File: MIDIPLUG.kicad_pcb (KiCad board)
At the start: 4 copper layers, 24.4 x 31.1 mm, 31 parts, among them J1 Joystick Port, P1 LINE OUT, U1 LP2985-3.3, U2 SAM2695, Y1 12Mhz

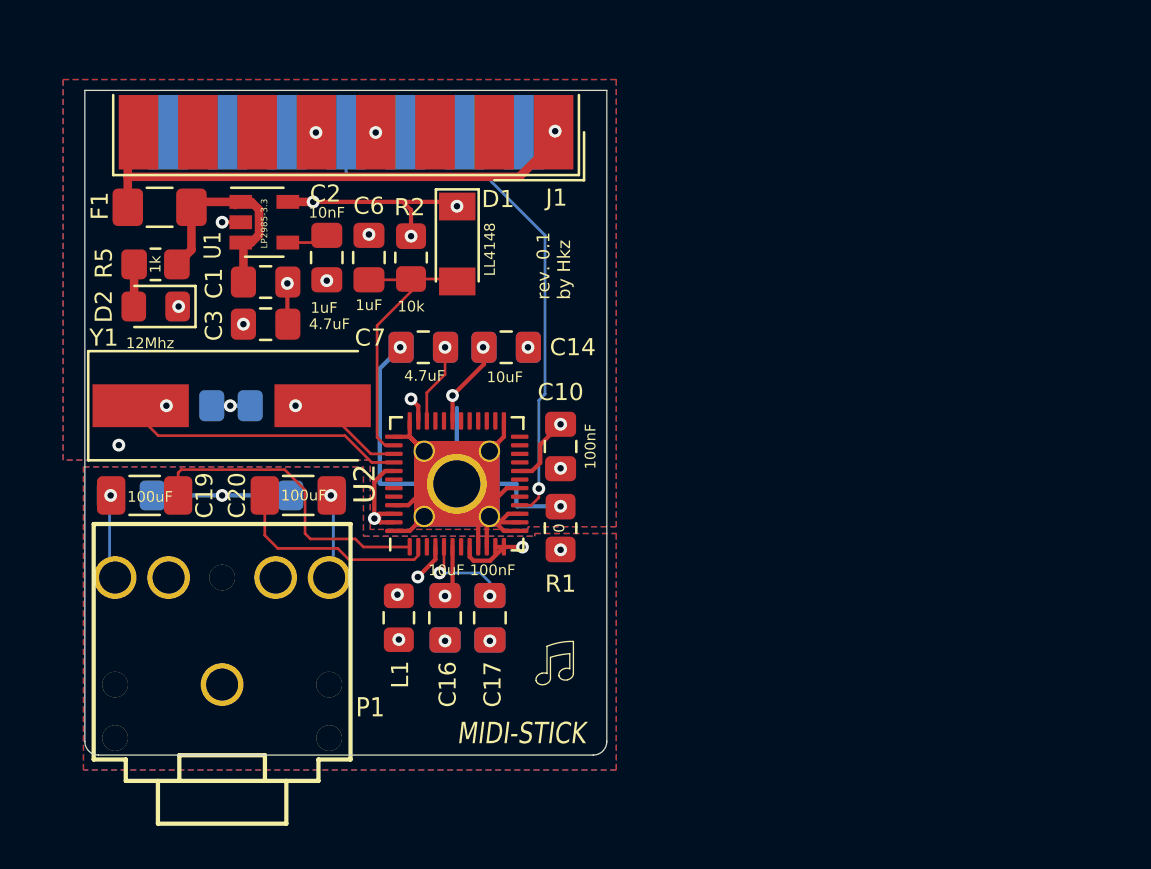
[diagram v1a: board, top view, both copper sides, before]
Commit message: Begin reorganizing board
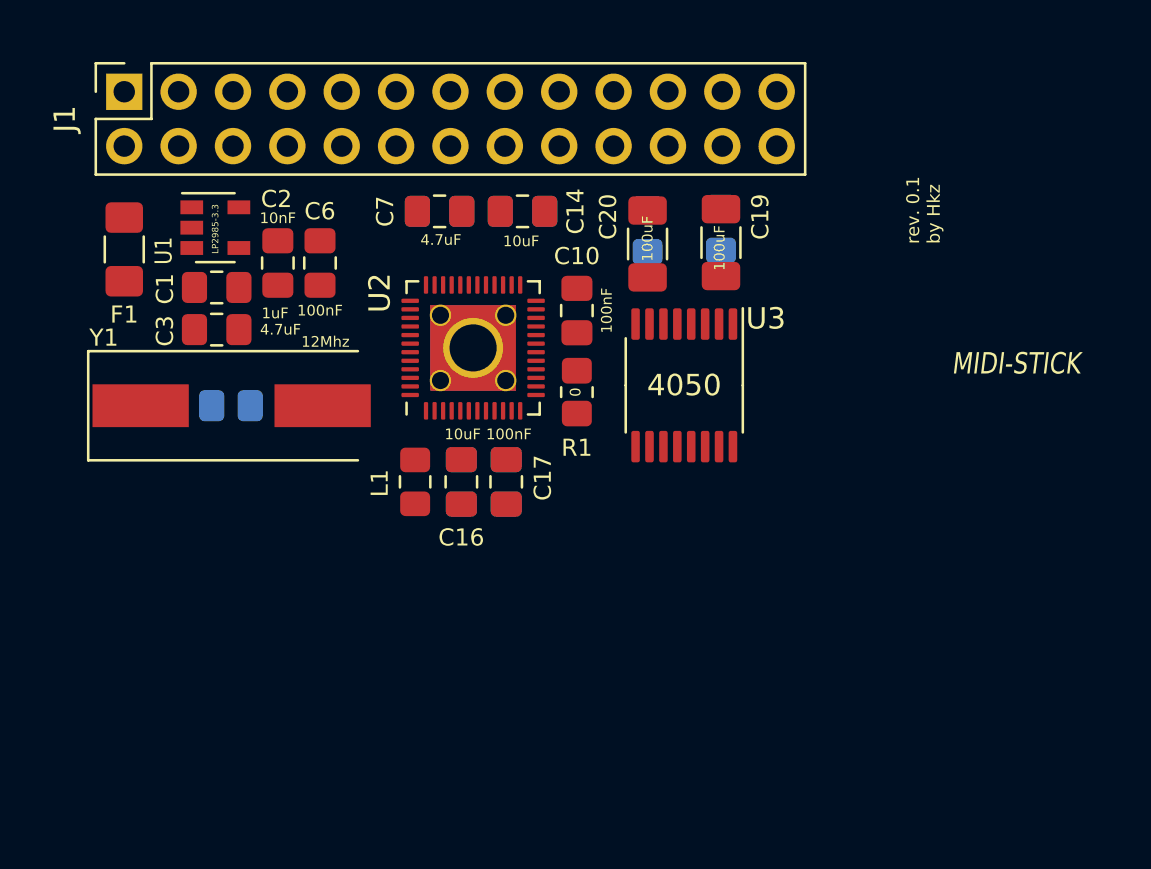
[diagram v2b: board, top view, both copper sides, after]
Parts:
- removed D1: LL4148, Diode_SMD:D_MiniMELF
- removed D2: Power, LED_SMD:LED_0805_2012Metric_Pad1.15x1.40mm_HandSolder
- removed P1: LINE OUT, My_Components:Conn_Audio_3.5mm_Stereo_SJ1-352XNG
- removed R2: 10k, Resistor_SMD:R_0805_2012Metric_Pad1.20x1.40mm_HandSolder
- removed R5: 1k, Resistor_SMD:R_0805_2012Metric_Pad1.20x1.40mm_HandSolder
- added U3: 4050, Package_SO:TSSOP-16_4.4x5mm_P0.65mm, F.Cu at (134.6, 88.1)
- C6: value 1uF -> 100nF
- J1: value Joystick Port -> Wavetable Connector; footprint Connector_Dsub:DSUB-15_Male_EdgeMount_P2.77mm -> Connector_PinSocket_2.54mm:PinSocket_2x13_P2.54mm_Vertical
- moved R4 30.2 mm to (136.3, 80.8), turned to 270 degrees
- moved C19 29.4 mm to (136.3, 81.5), turned to 90 degrees
- moved C20 20.1 mm to (132.9, 81.5), turned to 90 degrees
- moved R3 20.0 mm to (132.9, 80.9), turned to 270 degrees
- moved J1 10.5 mm to (108.5, 74.4), turned to 90 degrees
- moved C10 6.40 mm to (129.6, 84.6)
- moved U2 6.40 mm to (124.8, 86.4)
- moved C14 6.40 mm to (127.1, 80.0)
- moved C15 6.40 mm to (124.2, 92.6)
- moved C16 6.40 mm to (124.2, 92.6)
- moved C17 6.40 mm to (126.3, 92.6)
- moved C18 6.40 mm to (126.3, 92.6)
- moved C7 6.40 mm to (123.2, 80.0)
- moved C8 6.40 mm to (123.2, 80.0)
- moved C9 6.40 mm to (127.1, 80.0)
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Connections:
- C19 pad 2: Net-(C19-Pad2) -> /AOUT_L
- C20 pad 2: Net-(C20-Pad2) -> /AOUT_R
- J1 pad 1: VCC -> GND
- J1 pad 10: (no net) -> VCC
- J1 pad 11: (no net) -> GND
- J1 pad 12: /MIDI_IN -> (no net)
- J1 pad 14: (no net) -> VCC
- J1 pad 3: (no net) -> GND
- J1 pad 4: GND -> /MIDI_IN
- J1 pad 6: (no net) -> VCC
- J1 pad 7: (no net) -> GND
- J1 pad 8: VCC -> (no net)
- J1 pad 9: VCC -> GND
- R3 pad 1: Net-(C20-Pad2) -> /AOUT_R
- R4 pad 1: Net-(C19-Pad2) -> /AOUT_L
- U2 pad 16: /MIDI_IN -> Net-(U2-Pad16)
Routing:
- net GND: track 114.5 -> 0.00 mm, vias 13 -> 0
- net VDD: track 76.2 -> 0.00 mm, vias 11 -> 0
- net GNDA: track 39.5 -> 0.00 mm, vias 5 -> 0
- net VCC: track 26.2 -> 0.00 mm, vias 1 -> 0
- net /MIDI_IN: track 25.8 -> 0.00 mm, vias 1 -> 0
- net Net-(C19-Pad1): track 15.2 -> 0.00 mm
- net Net-(C5-Pad1): track 13.3 -> 0.00 mm, vias 1 -> 0
- net Net-(C6-Pad1): track 13.2 -> 0.00 mm
- net Net-(C1-Pad1): track 11.6 -> 0.00 mm
- net Net-(C20-Pad1): track 10.8 -> 0.00 mm
- net VDDA: track 5.85 -> 0.00 mm, vias 2 -> 0
- net Net-(C17-Pad1): track 4.44 -> 0.00 mm, vias 2 -> 0
- net Net-(C4-Pad1): track 4.25 -> 0.00 mm, vias 1 -> 0
- net Net-(C19-Pad2): track 3.94 -> 0.00 mm, vias 1 -> 0
- net Net-(C20-Pad2): track 3.91 -> 0.00 mm, vias 1 -> 0
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- removed copper zone on B.Cu, net GND
- removed copper zone on F.Cu, net GND
- removed copper zone on In1.Cu, net GND
- removed copper zone on B.Cu, net GNDA
- removed copper zone on F.Cu, net GNDA
- removed copper zone on In1.Cu, net GNDA
- removed copper zone on In2.Cu, net GNDA
- removed copper zone on In2.Cu, net VDD
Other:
- board outline removed

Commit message: Routed internal version
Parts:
- moved R1 2.22 mm to (129.6, 90.7)
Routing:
- net GND: track 0.00 -> 107.3 mm, vias 0 -> 6
- net VDD: track 0.00 -> 80.8 mm, vias 0 -> 7
- net GNDA: track 0.00 -> 47.0 mm, vias 0 -> 2
- net Net-(C20-Pad1): track 0.00 -> 42.0 mm, vias 0 -> 2
- net Net-(C19-Pad1): track 0.00 -> 40.5 mm, vias 0 -> 2
- net /MIDI_IN: track 0.00 -> 29.9 mm
- net Net-(C6-Pad1): track 0.00 -> 22.9 mm, vias 0 -> 2
- net VCC: track 0.00 -> 21.7 mm
- net Net-(C5-Pad1): track 0.00 -> 17.5 mm, vias 0 -> 1
- net /~RESET_5V: track 0.00 -> 14.7 mm
- net VDDA: track 0.00 -> 10.6 mm, vias 0 -> 2
- net Net-(U2-Pad16): track 0.00 -> 9.31 mm, vias 0 -> 2
- net Net-(C1-Pad1): track 0.00 -> 9.22 mm
- net Net-(C17-Pad1): track 0.00 -> 7.68 mm, vias 0 -> 2
- net Net-(C4-Pad1): track 0.00 -> 6.83 mm, vias 0 -> 1
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- added copper zone on B.Cu, net GND
- added copper zone on F.Cu, net GND
- added copper zone on B.Cu, net GNDA
- added copper zone on F.Cu, net GNDA
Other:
- board outline added: 34 x 23.4 mm
- copper layers 4 -> 2
- board text added: "DWAVE"
- board text removed: "MIDI-STICK"

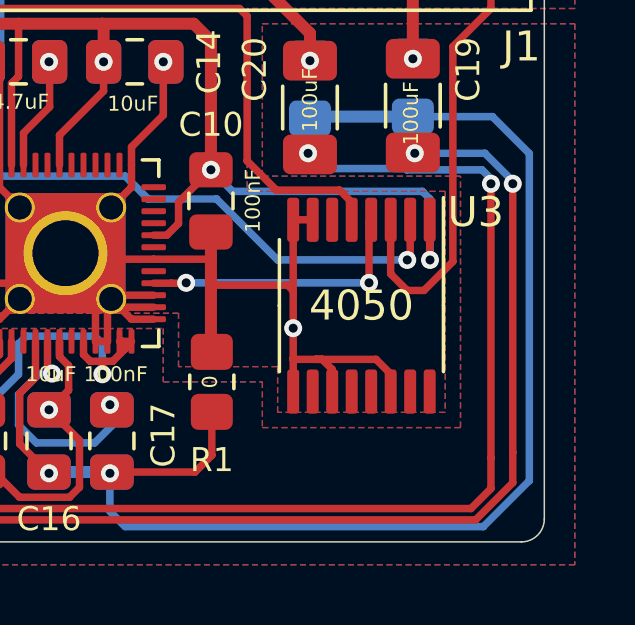
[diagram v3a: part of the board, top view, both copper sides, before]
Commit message: Add bypass cap for 4050
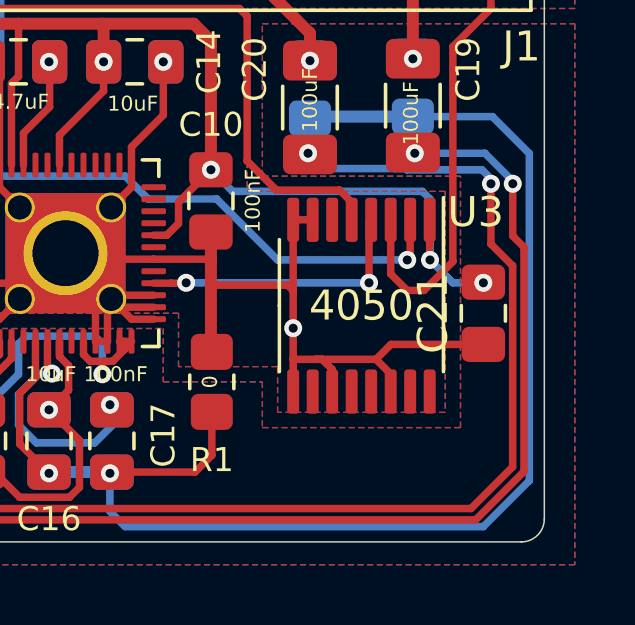
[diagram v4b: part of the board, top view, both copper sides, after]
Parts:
- added C21: 100nF, Capacitor_SMD:C_0805_2012Metric_Pad1.18x1.45mm_HandSolder, F.Cu at (138.7, 88.4)
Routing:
- net GND: track 107.3 -> 111.1 mm
- net VDD: track 80.8 -> 82.9 mm, vias 7 -> 8
- net Net-(C20-Pad1): track 42.0 -> 42.6 mm
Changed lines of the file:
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@@
     (thickness 1.6)
     (drawings 11)
-    (tracks 318)
+    (tracks 325)
     (zones 0)
-    (modules 27)
+    (modules 28)
     (nets 20)
   )
@@
     (add_net "Net-(C6-Pad1)")
     (add_net "Net-(C7-Pad2)")
+    (add_net "Net-(J1-Pad12)")
+    (add_net "Net-(J1-Pad13)")
+    (add_net "Net-(J1-Pad15)")
+    (add_net "Net-(J1-Pad16)")
+    (add_net "Net-(J1-Pad17)")
+    (add_net "Net-(J1-Pad18)")
+    (add_net "Net-(J1-Pad19)")
+    (add_net "Net-(J1-Pad2)")
+    (add_net "Net-(J1-Pad21)")
+    (add_net "Net-(J1-Pad22)")
+    (add_net "Net-(J1-Pad23)")
+    (add_net "Net-(J1-Pad25)")
+    (add_net "Net-(J1-Pad8)")
     (add_net "Net-(U2-Pad16)")
+    (add_net "Net-(U2-Pad24)")
+    (add_net "Net-(U2-Pad26)")
+    (add_net "Net-(U2-Pad27)")
+    (add_net "Net-(U2-Pad28)")
+    (add_net "Net-(U2-Pad29)")
     (add_net "Net-(U2-Pad3)")
+    (add_net "Net-(U2-Pad30)")
+    (add_net "Net-(U2-Pad32)")
+    (add_net "Net-(U2-Pad33)")
+    (add_net "Net-(U2-Pad42)")
     (add_net "Net-(U2-Pad7)")
     (add_net "Net-(U3-Pad10)")
@@
     (add_net VDD)
     (add_net VDDA)
+  )
+  (module Capacitor_SMD:C_0805_2012Metric_Pad1.18x1.45mm_HandSolder (layer F.Cu)
+    (at 138.684 88.392 90)
+    (descr "Capacitor SMD 0805 (2012 Metric), square (rectangular) end terminal, IPC_7351 nominal with elongated pad for handsoldering. (Body size source: IPC-SM-782 page 76, https://www.pcb-3d.com/wordpress/wp-content/uploads/ipc-sm-782a_amendment_1_and_2.pdf, https://docs.google.com/spreadsheets/d/1BsfQQcO9C6DZCsRaXUlFlo91Tg2WpOkGARC1WS5S8t0/edit?usp=sharing), generated with kicad-footprint-generator")
+    (tags "capacitor handsolder")
+    (attr smd)
+    (fp_text reference C21 (at 0 -1.68 90) (layer F.SilkS)
+      (effects (font (size 1 1) (thickness 0.15)))
+    )
+    (fp_text value 100nF (at 0 1.68 90) (layer F.Fab)
+      (effects (font (size 1 1) (thickness 0.15)))
+    )
+    (fp_text user %R (at 0 0 90) (layer F.Fab)
+      (effects (font (size 0.5 0.5) (thickness 0.08)))
+    )
+    (fp_line (start -1 0.625) (end -1 -0.625) (layer F.Fab) (width 0.1))
+    (fp_line (start -1 -0.625) (end 1 -0.625) (layer F.Fab) (width 0.1))
+    (fp_line (start 1 -0.625) (end 1 0.625) (layer F.Fab) (width 0.1))
+    (fp_line (start 1 0.625) (end -1 0.625) (layer F.Fab) (width 0.1))
+    (fp_line (start -0.261252 -0.735) (end 0.261252 -0.735) (layer F.SilkS) (width 0.12))
+    (fp_line (start -0.261252 0.735) (end 0.261252 0.735) (layer F.SilkS) (width 0.12))
+    (fp_line (start -1.88 0.98) (end -1.88 -0.98) (layer F.CrtYd) (width 0.05))
+    (fp_line (start -1.88 -0.98) (end 1.88 -0.98) (layer F.CrtYd) (width 0.05))
+    (fp_line (start 1.88 -0.98) (end 1.88 0.98) (layer F.CrtYd) (width 0.05))
+    (fp_line (start 1.88 0.98) (end -1.88 0.98) (layer F.CrtYd) (width 0.05))
+    (pad 2 smd roundrect (at 1.0375 0 90) (size 1.175 1.45) (layers F.Cu F.Paste F.Mask) (roundrect_rratio 0.212766)
+      (net 4 VDD))
+    (pad 1 smd roundrect (at -1.0375 0 90) (size 1.175 1.45) (layers F.Cu F.Paste F.Mask) (roundrect_rratio 0.212766)
+      (net 1 GND))
+    (model ${KISYS3DMOD}/Capacitor_SMD.3dshapes/C_0805_2012Metric.wrl
+      (at (xyz 0 0 0))
+      (scale (xyz 1 1 1))
+      (rotate (xyz 0 0 0))
+    )
   )
   (module Package_SO:TSSOP-16_4.4x5mm_P0.65mm (layer F.Cu)
@@
     (effects (font (size 0.6 0.6) (thickness 0.1)) (justify left mirror))
   )
+  (via (at 138.684 87.376) (size 0.6) (drill 0.3) (layers F.Cu B.Cu) (net 4))
   (via (at 122.174 93.472) (size 0.6) (drill 0.3) (layers F.Cu B.Cu) (net 9))
   (via (at 122.174 91.44) (size 0.6) (drill 0.3) (layers F.Cu B.Cu) (net 4))
@@
   (segment (start 132.345 88.889) (end 132.345 87.641) (width 0.25) (layer F.Cu) (net 1))
   (via (at 132.345 88.889) (size 0.6) (drill 0.3) (layers F.Cu B.Cu) (net 1))
+  (segment (start 135.60432 89.4295) (end 135.10682 89.927) (width 0.25) (layer F.Cu) (net 1))
+  (segment (start 138.684 89.4295) (end 135.60432 89.4295) (width 0.25) (layer F.Cu) (net 1))
   (segment (start 108.458 83.2755) (end 108.6755 83.2755) (width 0.4) (layer F.Cu) (net 2))
   (segment (start 108.966 83.566) (end 111.7385 83.566) (width 0.4) (layer F.Cu) (net 2))
@@
   (segment (start 125.984 89.408) (end 125.984 90.424) (width 0.25) (layer B.Cu) (net 4))
   (segment (start 125.73 89.154) (end 125.984 89.408) (width 0.25) (layer B.Cu) (net 4))
+  (segment (start 137.668 87.376) (end 136.906 86.614) (width 0.25) (layer B.Cu) (net 4))
+  (segment (start 138.684 87.376) (end 137.668 87.376) (width 0.25) (layer B.Cu) (net 4))
   (segment (start 117.7245 89.0905) (end 118.4275 89.0905) (width 0.127) (layer F.Cu) (net 5))
   (segment (start 120.14199 87.37601) (end 120.14199 85.59801) (width 0.127) (layer F.Cu) (net 5))
@@
   (segment (start 140.217004 83.067004) (end 140.217004 93.970996) (width 0.25) (layer B.Cu) (net 10))
   (segment (start 138.9855 81.8355) (end 140.217004 83.067004) (width 0.25) (layer B.Cu) (net 10))
-  (segment (start 140.217004 93.970996) (end 138.684 95.504) (width 0.25) (layer B.Cu) (net 10))
   (segment (start 138.684 95.504) (end 126.746 95.504) (width 0.25) (layer B.Cu) (net 10))
   (segment (start 126.238 94.996) (end 126.238 93.726) (width 0.25) (layer B.Cu) (net 10))
@@
   (segment (start 129.074 93.684) (end 129.6335 93.1245) (width 0.25) (layer F.Cu) (net 10))
   (segment (start 126.3015 93.684) (end 124.206 93.684) (width 0.4) (layer B.Cu) (net 10))
+  (segment (start 140.217004 93.970996) (end 138.684 95.504) (width 0.25) (layer B.Cu) (net 10))
   (via (at 124.3075 90.402695) (size 0.6) (drill 0.3) (layers F.Cu B.Cu) (net 11))
   (segment (start 124.1555 90.250695) (end 124.3075 90.402695) (width 0.25) (layer F.Cu) (net 11))
@@
   (segment (start 138.738962 83.058) (end 139.665003 83.984041) (width 0.25) (layer B.Cu) (net 12))
   (segment (start 136.398 83.058) (end 138.738962 83.058) (width 0.25) (layer B.Cu) (net 12))
-  (segment (start 138.427643 95.277529) (end 139.665003 94.040169) (width 0.25) (layer F.Cu) (net 12))
   (segment (start 120.52699 90.775838) (end 120.526991 94.898163) (width 0.25) (layer F.Cu) (net 12))
   (segment (start 120.885347 90.417481) (end 120.52699 90.775838) (width 0.25) (layer F.Cu) (net 12))
-  (segment (start 139.665003 93.024169) (end 139.665003 84.074) (width 0.25) (layer F.Cu) (net 12))
   (segment (start 120.906358 95.27753) (end 138.427643 95.277529) (width 0.25) (layer F.Cu) (net 12))
   (segment (start 121.901348 90.41748) (end 120.885347 90.417481) (width 0.25) (layer F.Cu) (net 12))
-  (segment (start 139.665003 94.040169) (end 139.665003 93.024169) (width 0.25) (layer F.Cu) (net 12))
   (segment (start 120.526991 94.898163) (end 120.906358 95.27753) (width 0.25) (layer F.Cu) (net 12))
   (segment (start 122.5555 89.763328) (end 121.901348 90.41748) (width 0.25) (layer F.Cu) (net 12))
   (segment (start 122.5555 89.329) (end 122.5555 89.763328) (width 0.25) (layer F.Cu) (net 12))
+  (segment (start 140.03802 93.667152) (end 140.03802 86.19002) (width 0.25) (layer F.Cu) (net 12))
+  (segment (start 138.427643 95.277529) (end 140.03802 93.667152) (width 0.25) (layer F.Cu) (net 12))
+  (segment (start 139.665003 85.817003) (end 139.665003 84.074) (width 0.25) (layer F.Cu) (net 12))
+  (segment (start 140.03802 86.19002) (end 139.665003 85.817003) (width 0.25) (layer F.Cu) (net 12))
   (segment (start 132.842 83.058) (end 133.35 83.566) (width 0.25) (layer B.Cu) (net 13))
   (segment (start 136.133039 83.610001) (end 138.639999 83.610001) (width 0.25) (layer B.Cu) (net 13))
@@
   (segment (start 138.938 83.908002) (end 138.938 84.074) (width 0.25) (layer B.Cu) (net 13))
   (segment (start 138.639999 83.610001) (end 138.938 83.908002) (width 0.25) (layer B.Cu) (net 13))
-  (segment (start 138.938 93.218) (end 138.938 84.074) (width 0.25) (layer F.Cu) (net 13))
-  (segment (start 138.938 94.234) (end 138.938 93.218) (width 0.25) (layer F.Cu) (net 13))
   (segment (start 121.06252 94.90052) (end 138.27148 94.90052) (width 0.25) (layer F.Cu) (net 13))
   (segment (start 120.904 94.742) (end 121.06252 94.90052) (width 0.25) (layer F.Cu) (net 13))
@@
   (segment (start 122.05751 90.79449) (end 121.04151 90.79449) (width 0.25) (layer F.Cu) (net 13))
   (segment (start 122.9555 89.8965) (end 122.05751 90.79449) (width 0.25) (layer F.Cu) (net 13))
-  (segment (start 138.27148 94.90052) (end 138.938 94.234) (width 0.25) (layer F.Cu) (net 13))
   (segment (start 122.9555 89.329) (end 122.9555 89.8965) (width 0.25) (layer F.Cu) (net 13))
+  (segment (start 139.66101 93.51099) (end 138.27148 94.90052) (width 0.25) (layer F.Cu) (net 13))
+  (segment (start 139.66101 86.809058) (end 139.66101 93.51099) (width 0.25) (layer F.Cu) (net 13))
+  (segment (start 138.938 86.086048) (end 139.66101 86.809058) (width 0.25) (layer F.Cu) (net 13))
+  (segment (start 138.938 84.074) (end 138.938 86.086048) (width 0.25) (layer F.Cu) (net 13))
   (segment (start 108.458 80.3005) (end 108.458 79.502) (width 0.4) (layer F.Cu) (net 14))
   (segment (start 109.820999 78.139001) (end 109.820999 76.361001) (width 0.4) (layer F.Cu) (net 14))

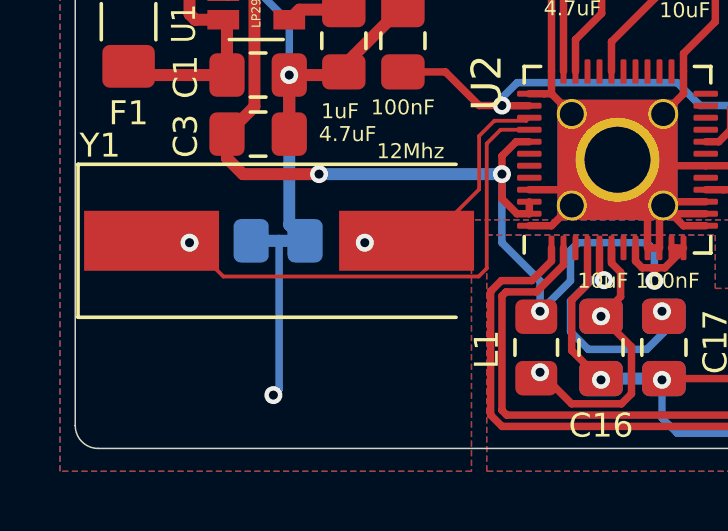
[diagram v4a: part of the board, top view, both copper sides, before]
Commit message: Moved around some components
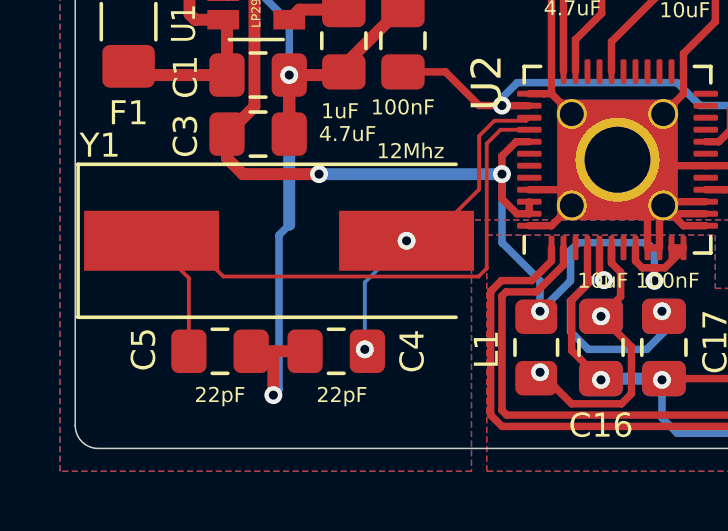
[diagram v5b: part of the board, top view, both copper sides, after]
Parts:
- C4, C5: moved to F.Cu
- moved C4 3.68 mm to (115.4, 92.8)
- moved C5 3.68 mm to (111.5, 92.8)
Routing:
- net Net-(C5-Pad1): track 17.5 -> 21.7 mm, vias 1 -> 0
- net Net-(C4-Pad1): track 6.83 -> 11.0 mm, vias 1 -> 2
- net GND: track 111.1 -> 112.5 mm
